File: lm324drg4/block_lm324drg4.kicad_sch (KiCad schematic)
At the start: 11 parts, among them U1 LM324DRG4

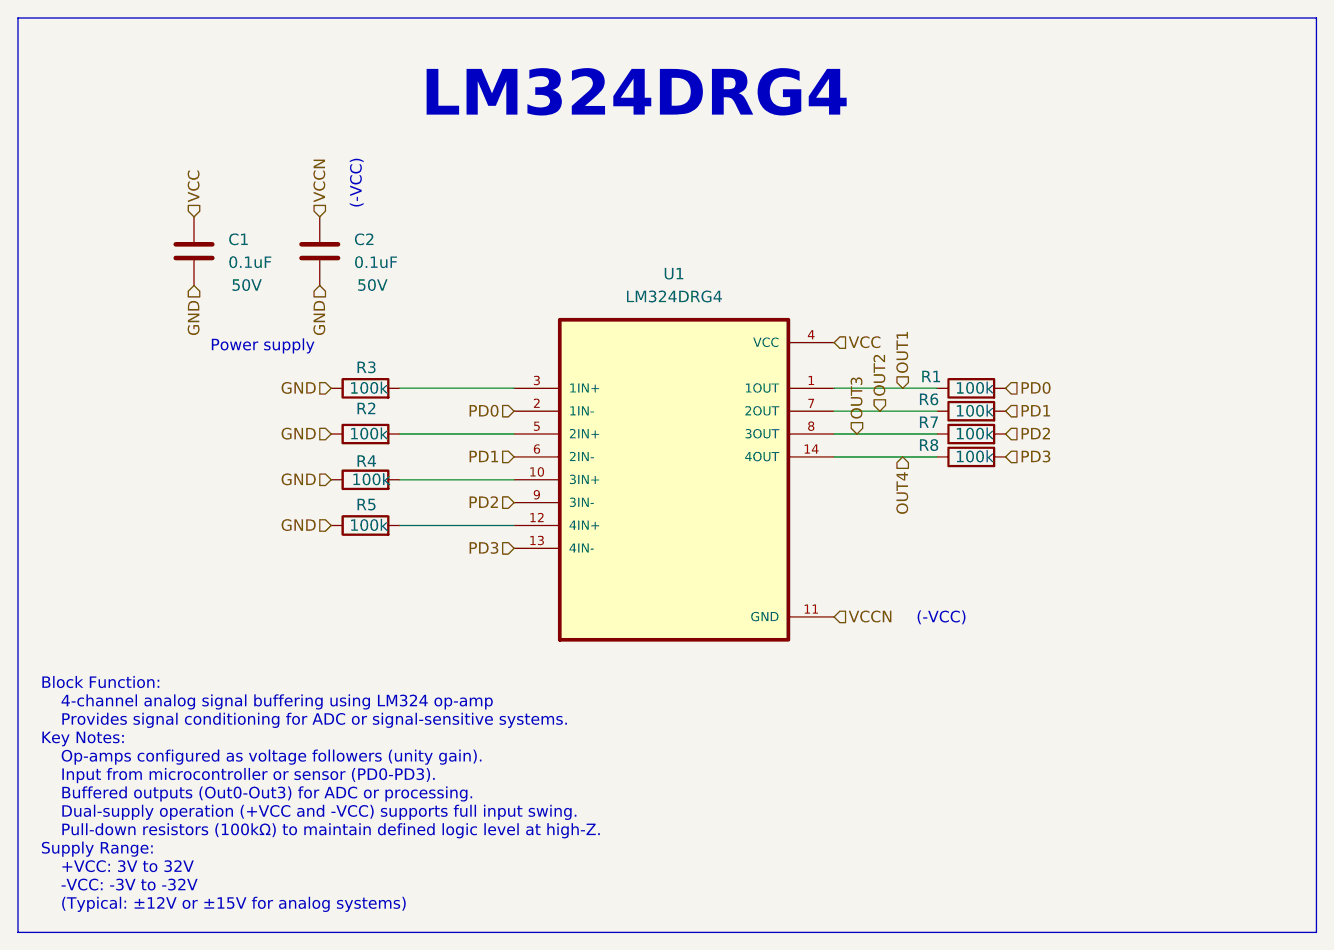
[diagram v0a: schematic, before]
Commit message: [Rushil] changed vccn to vee
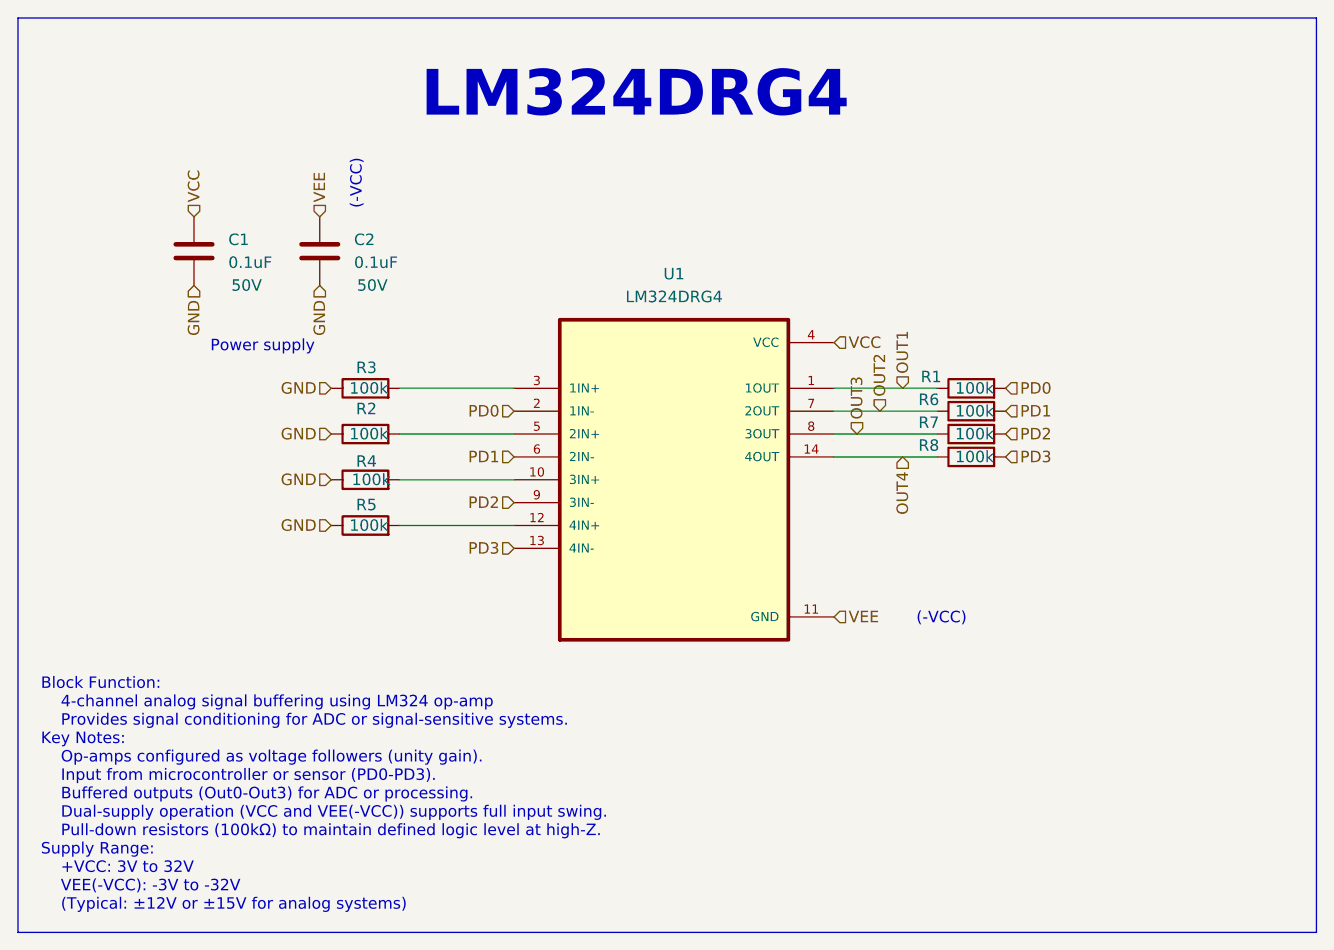
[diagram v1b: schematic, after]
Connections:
- net VCCN renamed VEE
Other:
- note added: "Block Function: 4-channel analog signal buffering using LM324 op-amp Provides signal conditioning for ADC or signal-sensitive systems. Key Notes: Op-amps configured as voltage followers (unity gain). Input from microcontroller or sensor (PD0-PD3). Buffered outputs (Out0-Out3) for ADC or processing. Dual-supply operation (VCC and VEE(-VCC)) supports full input swing. Pull-down resistors (100kΩ) to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"
- note removed: "Block Function: 4-channel analog signal buffering using LM324 op-amp Provides signal conditioning for ADC or signal-sensitive systems. Key Notes: Op-amps configured as voltage followers (unity gain). Input from microcontroller or sensor (PD0-PD3). Buffered outputs (Out0-Out3) for ADC or processing. Dual-supply operation (+VCC and -VCC) supports full input swing. Pull-down resistors (100kΩ) to mai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"
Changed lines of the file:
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@@
 		)
 	)
-	(text "Block Function:\n    4-channel analog signal buffering using LM324 op-amp\n    Provides signal conditioning for ADC or signal-sensitive systems.\nKey Notes:\n    Op-amps configured as voltage followers (unity gain).\n    Input from microcontroller or sensor (PD0-PD3).\n    Buffered outputs (Out0-Out3) for ADC or processing.\n    Dual-supply operation (+VCC and -VCC) supports full input swing.\n    Pull-down resistors (100kΩ) to maintain defined logic level at high-Z.\nSupply Range:\n    +VCC: 3V to 32V\n    -VCC: -3V to -32V\n    (Typical: ±12V or ±15V for analog systems)"
+	(text "Block Function:\n    4-channel analog signal buffering using LM324 op-amp\n    Provides signal conditioning for ADC or signal-sensitive systems.\nKey Notes:\n    Op-amps configured as voltage followers (unity gain).\n    Input from microcontroller or sensor (PD0-PD3).\n    Buffered outputs (Out0-Out3) for ADC or processing.\n    Dual-supply operation (VCC and VEE(-VCC)) supports full input swing.\n    Pull-down resistors (100kΩ) to maintain defined logic level at high-Z.\nSupply Range:\n    +VCC: 3V to 32V\n    VEE(-VCC): -3V to -32V\n    (Typical: ±12V or ±15V for analog systems)"
 		(exclude_from_sim no)
 		(at 84.582 130.302 0)
@@
 		)
 	)
-	(hierarchical_label "VCCN"
+	(hierarchical_label "VEE"
 		(shape input)
 		(at 172.72 110.49 0)
@@
 		)
 	)
-	(hierarchical_label "VCCN"
+	(hierarchical_label "VEE"
 		(shape input)
 		(at 115.57 66.04 90)
